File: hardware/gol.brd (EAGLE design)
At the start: 59.7 x 59.7 mm, 69 parts, among them J1 TC2050-IDC, J2 2057-MCR-B-S-RA-TSMT-NP-CS4-T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, U1 STM32F072CBT, U2 AP2111H-3.3TRG1SOT-223_DIO-M

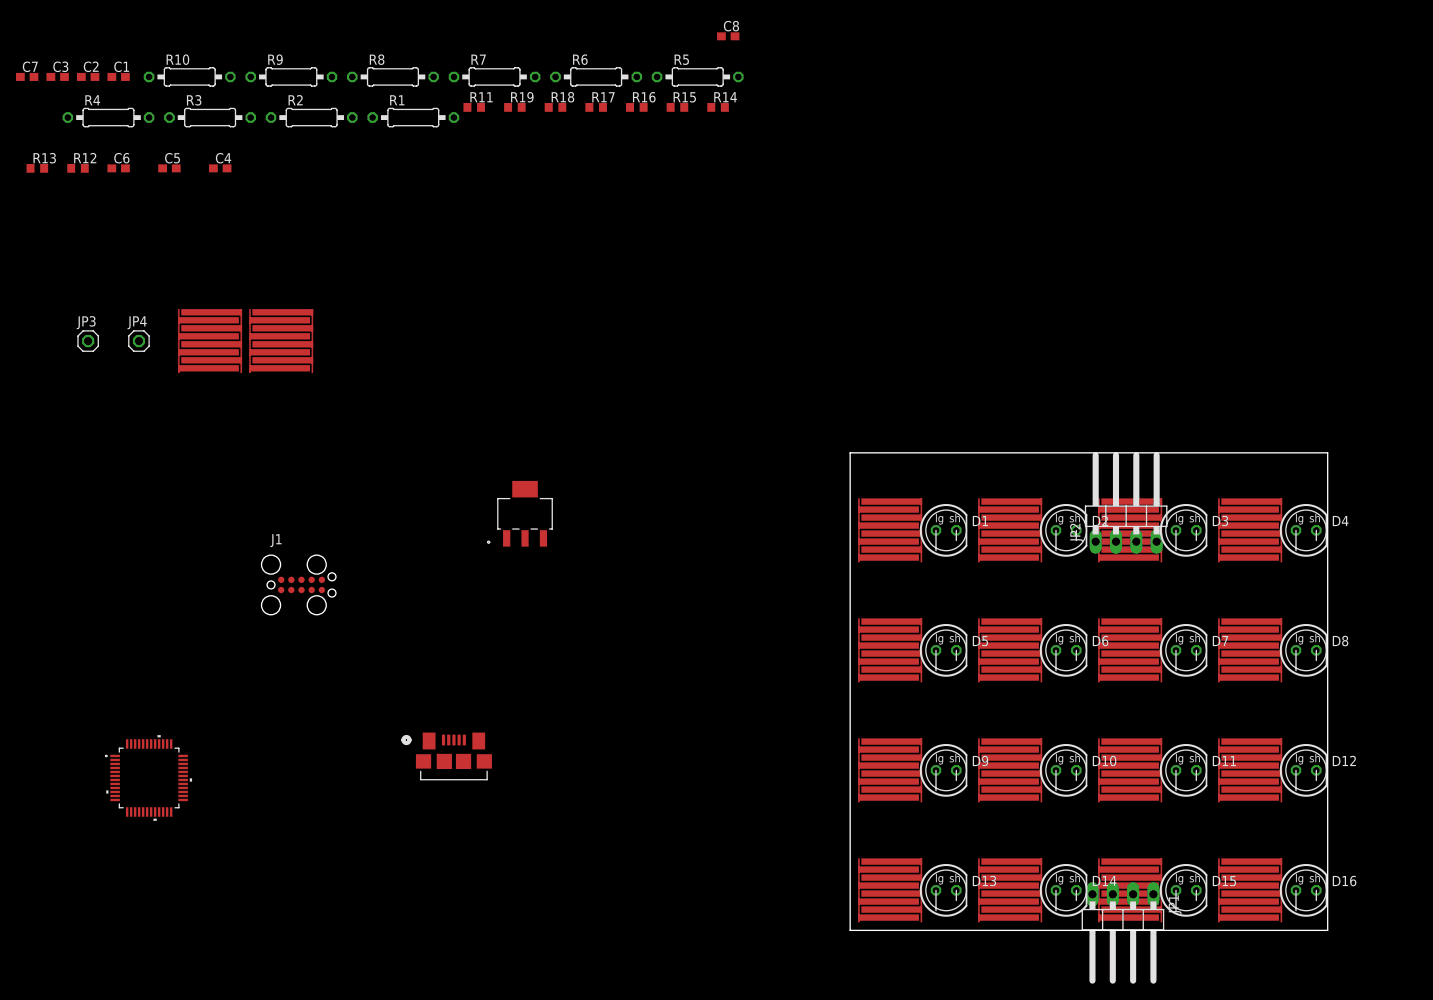
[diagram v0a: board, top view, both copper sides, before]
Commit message: Completes layout of top side components. Adds +12V grid horizontally.
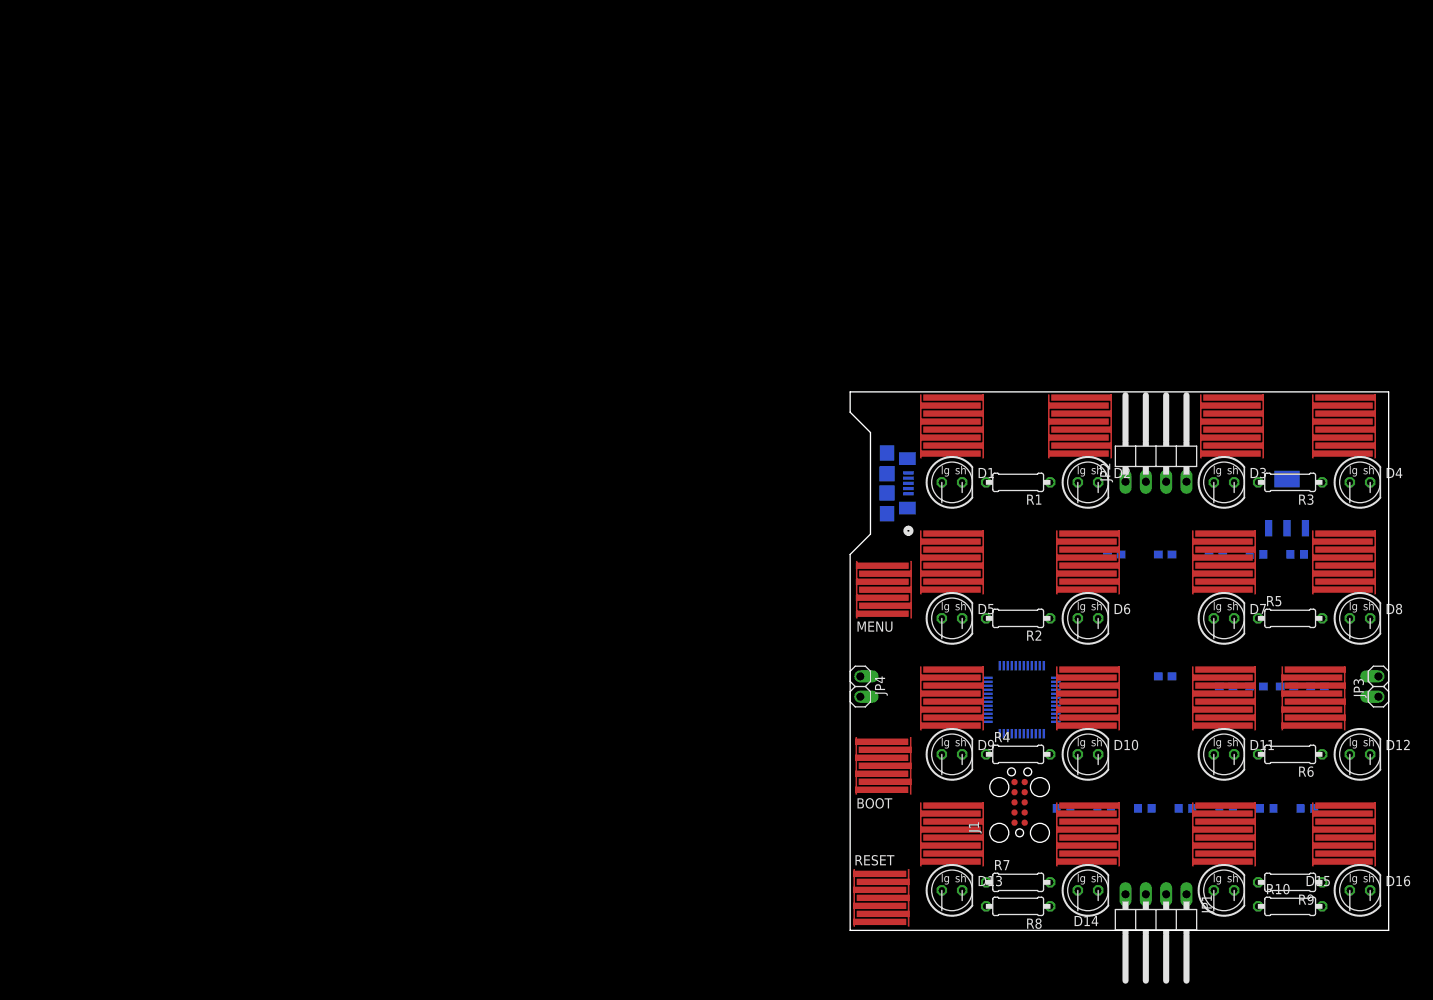
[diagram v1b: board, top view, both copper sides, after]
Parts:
- added BTN19: RESET, parts:COMB_EXPOSED
- BTN17: value BUTTON-RES -> BOOT
- BTN18: value BUTTON-RES -> MENU
- JP3, JP4: device pinhead:1X01 -> parts:1X02
- R1, R10, R2, R3, R4, R5, R6, R7, R8, R9: value (none) -> R-EU-0207/8; device rcl:0207/10 -> parts:0207/8
- moved C7 178.4 mm to (58.4, 30.5), flipped to the bottom
- moved R10 172.2 mm to (55.0, 3.00)
- moved C3 171.5 mm to (54.6, 30.5), flipped to the bottom
- moved JP3 167.0 mm to (66.0, 30.5), turned to 90 degrees
- moved C2 164.7 mm to (50.8, 30.5), flipped to the bottom
- moved R13 164.7 mm to (55.9, 47.0), flipped to the bottom
- moved R9 160.4 mm to (55.0, 6.00), turned to 180 degrees
- moved C1 158.0 mm to (47.0, 30.5), flipped to the bottom
- moved R12 155.0 mm to (50.8, 47.0), flipped to the bottom
- moved C6 145.4 mm to (45.7, 47.0), flipped to the bottom
- moved R3 142.5 mm to (55.0, 56.0), turned to 180 degrees
- moved R4 138.8 mm to (21.0, 22.0)
- moved R11 136.1 mm to (57.1, 15.2), flipped to the bottom
- moved C5 133.5 mm to (39.4, 47.0), flipped to the bottom
- moved R8 129.8 mm to (21.0, 3.00), turned to 180 degrees
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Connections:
- new net +12V: JP3.1, JP4.2
- net EAST: now also JP3.2; no longer JP3.1
- net GND: now also BTN19.P$2
- net NRST: now also BTN19.P$1
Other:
- board size 59.7 x 59.7 mm -> 67.3 x 67.3 mm

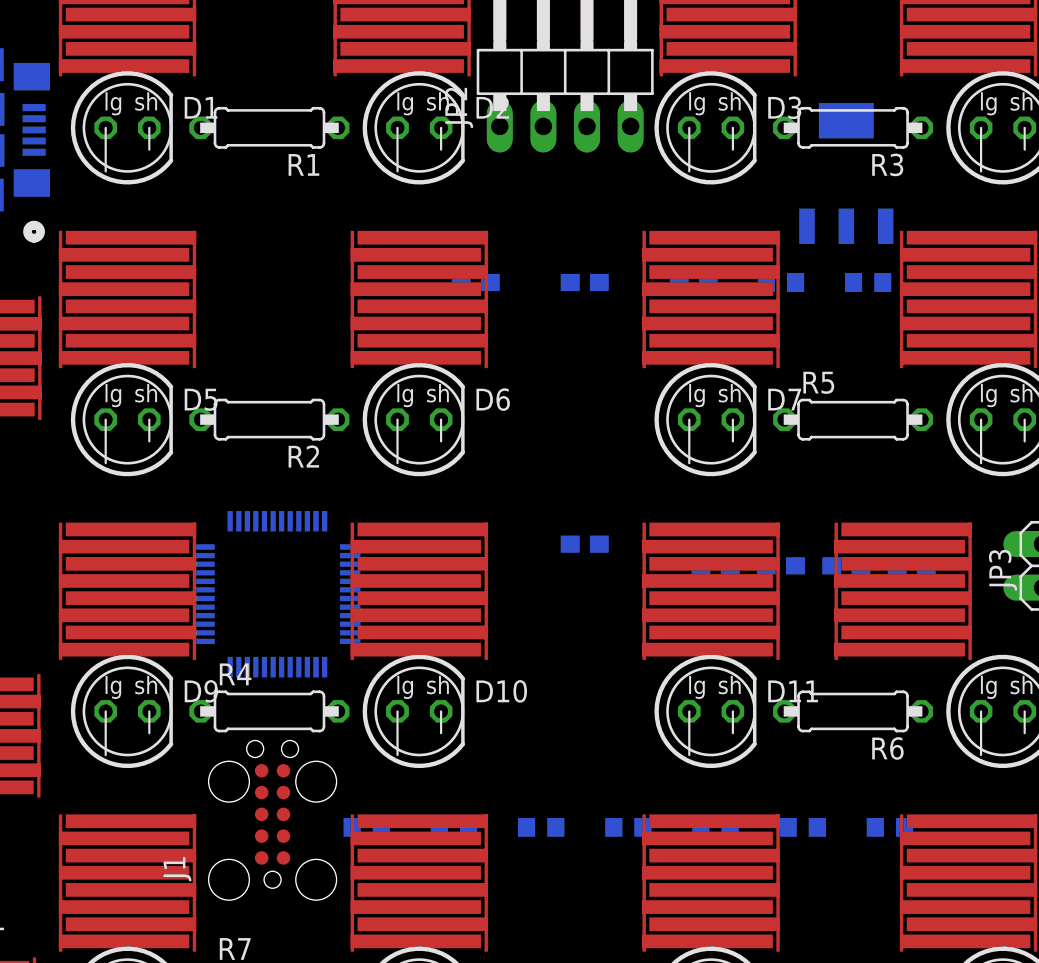
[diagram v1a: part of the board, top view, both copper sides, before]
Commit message: Completes part of the layout and a small part of the routing around the MCU.
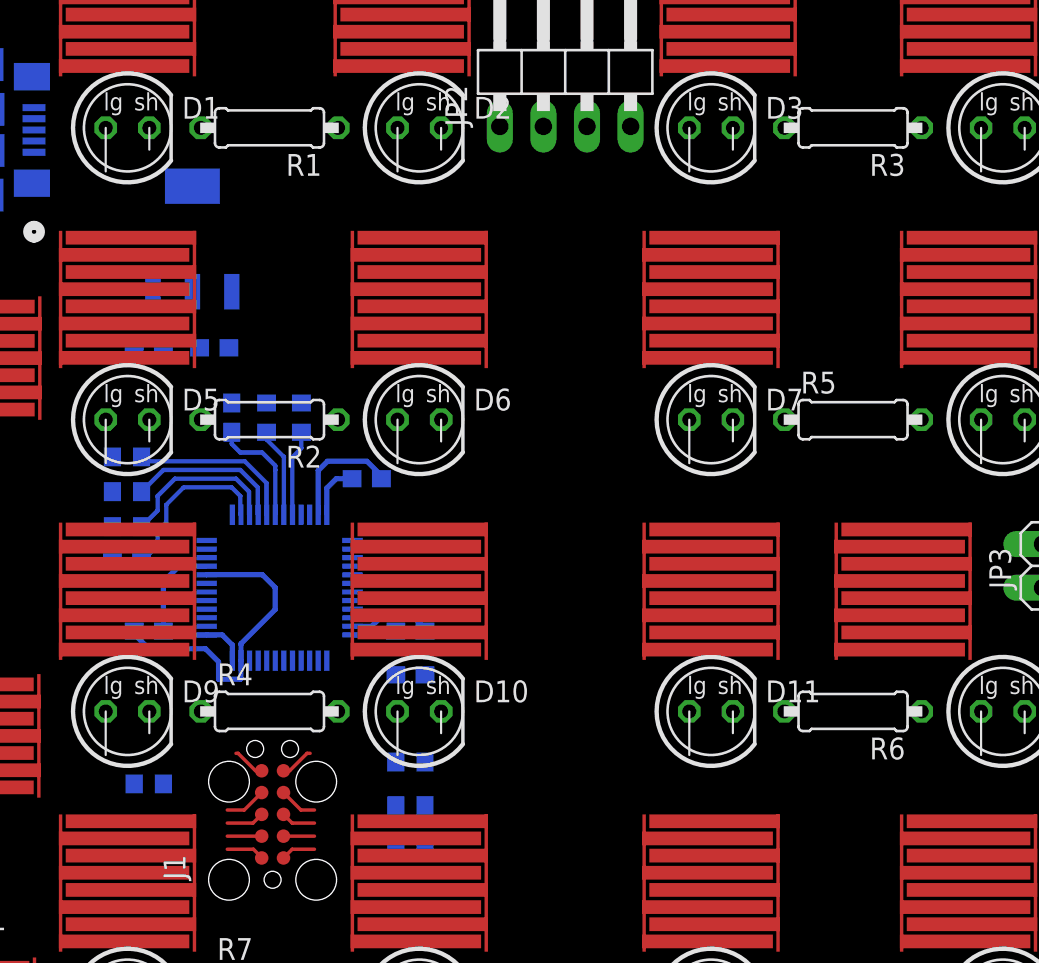
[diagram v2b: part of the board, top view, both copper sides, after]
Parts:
- moved R11 47.8 mm to (12.7, 32.8)
- moved R12 47.0 mm to (14.0, 17.8)
- moved C7 46.2 mm to (14.0, 43.2), turned to 180 degrees
- moved R13 44.9 mm to (12.7, 34.8)
- moved C3 40.8 mm to (14.0, 26.7), turned to 180 degrees
- moved U2 38.3 mm to (16.5, 49.5)
- moved C6 28.2 mm to (29.2, 24.1)
- moved R16 27.7 mm to (22.9, 39.1), turned to 270 degrees
- moved R15 26.3 mm to (20.8, 39.1), turned to 90 degrees
- moved C4 26.0 mm to (12.7, 30.7), turned to 180 degrees
- moved R14 25.7 mm to (12.7, 36.8)
- moved C2 24.7 mm to (26.7, 35.6)
- moved C8 24.4 mm to (17.8, 43.2)
- moved R19 22.9 mm to (29.2, 14.0)
- moved C5 22.0 mm to (18.8, 39.1), turned to 270 degrees
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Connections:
- net N$10 renamed OUTB-L1
- net N$11 renamed OUTB-L2
- net N$12 renamed OUTB-L3
- net N$16 renamed OUTD13
- net N$17 renamed OUTD14
- net N$20 renamed OUTD15
- net N$21 renamed OUTD16
- net N$7 renamed OUTA-L2
- net N$8 renamed OUTA-L1
- net N$9 renamed OUTA-L3
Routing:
- net GND: track 0.00 -> 32.6 mm
- net V+: track 0.00 -> 18.9 mm
- net N$1: track 0.00 -> 9.94 mm
- net ROW2: track 0.00 -> 9.76 mm
- net ROW0: track 0.00 -> 9.58 mm
- net ROW1: track 0.00 -> 9.32 mm
- net N$2: track 0.00 -> 6.61 mm
- net ROW3: track 0.00 -> 5.23 mm
- net COL0: track 0.00 -> 5.02 mm
- net PB7: track 0.00 -> 2.43 mm
- net NRST: track 0.00 -> 2.23 mm
- net SWDCLK: track 0.00 -> 2.23 mm
- net WEST: track 0.00 -> 2.22 mm
- net BOOT0: track 0.00 -> 2.00 mm
- net PB15: track 0.00 -> 1.97 mm
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
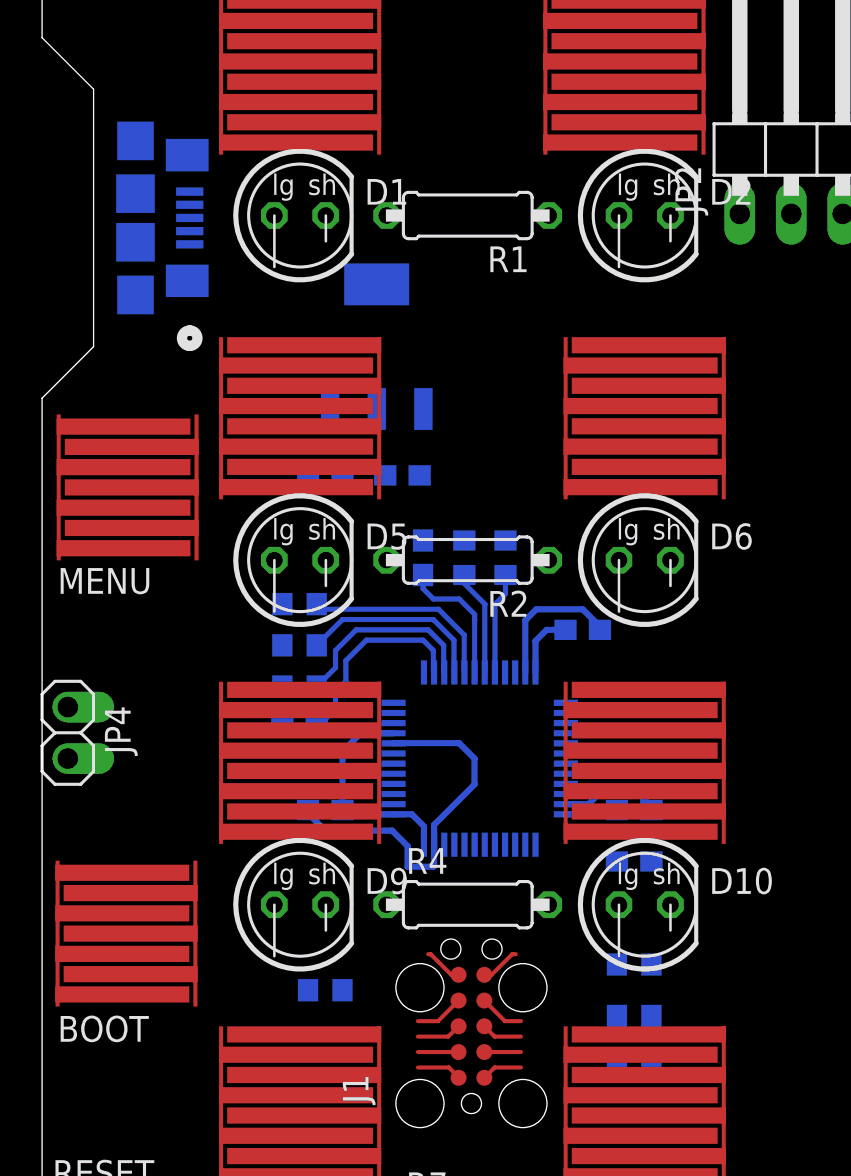
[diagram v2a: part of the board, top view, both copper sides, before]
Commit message: Adds edge-of-board to the mini-usb connector. Routes the USB lines.
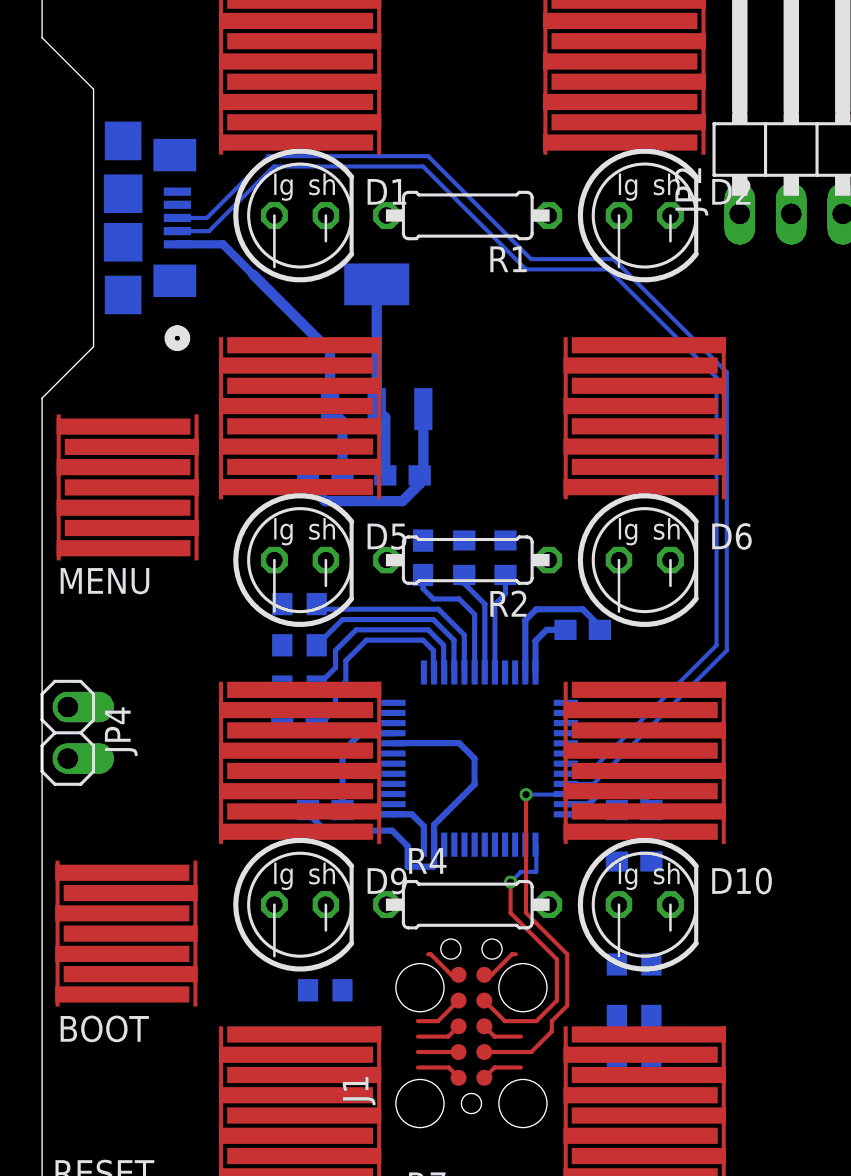
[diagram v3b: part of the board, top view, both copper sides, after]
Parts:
- moved J2 0.61 mm to (4.47, 55.9)
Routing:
- net USB_DP: track 0.00 -> 57.2 mm
- net USB_DM: track 0.00 -> 55.5 mm
- net SWDIO: track 1.80 -> 18.6 mm, vias 0 -> 1
- net +5V: track 0.00 -> 16.1 mm
- net SWDCLK: track 2.23 -> 14.1 mm, vias 0 -> 1
- net GND: track 32.6 -> 43.0 mm
- net V+: track 18.9 -> 28.5 mm

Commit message: more routing
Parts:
- moved BTN19 0.25 mm to (4.06, 4.06), turned to 180 degrees
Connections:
- net OUTB-L1: now also U1.38; no longer U1.29
- net OUTB-L2: now also U1.29; no longer U1.38
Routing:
- net NRST: track 2.23 -> 24.1 mm
- net COL3: track 0.00 -> 15.7 mm
- net COL2: track 0.00 -> 12.8 mm
- net COL1: track 0.00 -> 10.0 mm
- net BOOT0: track 2.00 -> 9.07 mm, vias 0 -> 1
- net N$3: track 0.00 -> 6.92 mm
- net OUTB-L1: track 0.00 -> 5.57 mm
- net GND: track 43.0 -> 48.2 mm
- net PB7: track 2.43 -> 4.72 mm

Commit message: more routing
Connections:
- net EAST: now also U1.21, U1.22; no longer U1.10, U1.11
- net WEST: now also U1.10, U1.11; no longer U1.21, U1.22
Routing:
- net CAN_TR: track 0.00 -> 76.4 mm, vias 0 -> 3
- net GND: track 48.2 -> 107.4 mm
- net +5V: track 16.1 -> 70.7 mm
- net N$13: track 0.00 -> 44.1 mm
- net WEST: track 2.22 -> 44.7 mm, vias 0 -> 3
- net N$15: track 0.00 -> 40.8 mm
- net BOOT0: track 9.07 -> 34.3 mm, vias 1 -> 2
- net NRST: track 24.1 -> 44.0 mm, vias 0 -> 1
- net EAST: track 1.92 -> 18.5 mm, vias 0 -> 1
- net PB15: track 1.97 -> 16.3 mm, vias 0 -> 1
- net PB7: track 4.72 -> 15.0 mm, vias 0 -> 1
- net OUTD14: track 0.00 -> 7.85 mm, vias 0 -> 1
- net OUTD13: track 0.00 -> 4.75 mm, vias 0 -> 1
- net OUTA-L3: track 0.00 -> 3.89 mm, vias 0 -> 1
- net NORTH: track 0.00 -> 2.65 mm

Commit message: more routing work
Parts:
- moved BTN1 0.51 mm to (12.7, 62.5)
- moved BTN2 0.51 mm to (28.7, 62.5)
- moved BTN3 0.51 mm to (47.7, 62.5)
- moved BTN4 0.51 mm to (61.7, 62.5)
- moved BTN19 0.36 mm to (4.32, 4.32)
- turned R5 to 180 degrees
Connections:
- net OUTB-L2: now also U1.25; no longer U1.29
- net OUTB-L3: now also U1.29; no longer U1.25
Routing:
- net GND: track 107.4 -> 287.5 mm, vias 0 -> 7
- net V+: track 28.4 -> 195.8 mm, vias 0 -> 8
- net IN_ROW0: track 0.00 -> 111.4 mm, vias 0 -> 7
- net IN_COL3: track 0.00 -> 85.7 mm, vias 0 -> 9
- net IN_ROW1: track 0.00 -> 81.5 mm, vias 0 -> 3
- net IN_ROW3: track 0.00 -> 70.1 mm, vias 0 -> 2
- net IN_COL0: track 0.00 -> 54.0 mm
- net OUTD15: track 0.00 -> 52.3 mm, vias 0 -> 3
- net IN_COL1: track 0.00 -> 49.9 mm, vias 0 -> 6
- net IN_ROW2: track 0.00 -> 49.4 mm, vias 0 -> 2
- net SOUTH: track 0.00 -> 42.9 mm, vias 0 -> 5
- net OUTB-L2: track 0.00 -> 29.3 mm, vias 0 -> 3
- net +5V: track 70.7 -> 94.7 mm, vias 0 -> 1
- net OUTB-L3: track 0.00 -> 19.3 mm, vias 0 -> 3
- net OUTD16: track 0.00 -> 19.3 mm, vias 0 -> 3
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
